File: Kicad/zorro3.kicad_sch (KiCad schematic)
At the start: 13 parts, among them CN1 Zorro3, U1 SN74ABT16543DGGR, U2 SN74ABT16543DGGR, U3 SN74ABT16543DGGR, U4 SN74ABT16543DGGR, U5 74LVC07APW_118, U6 SN74ABT16245ADGGR

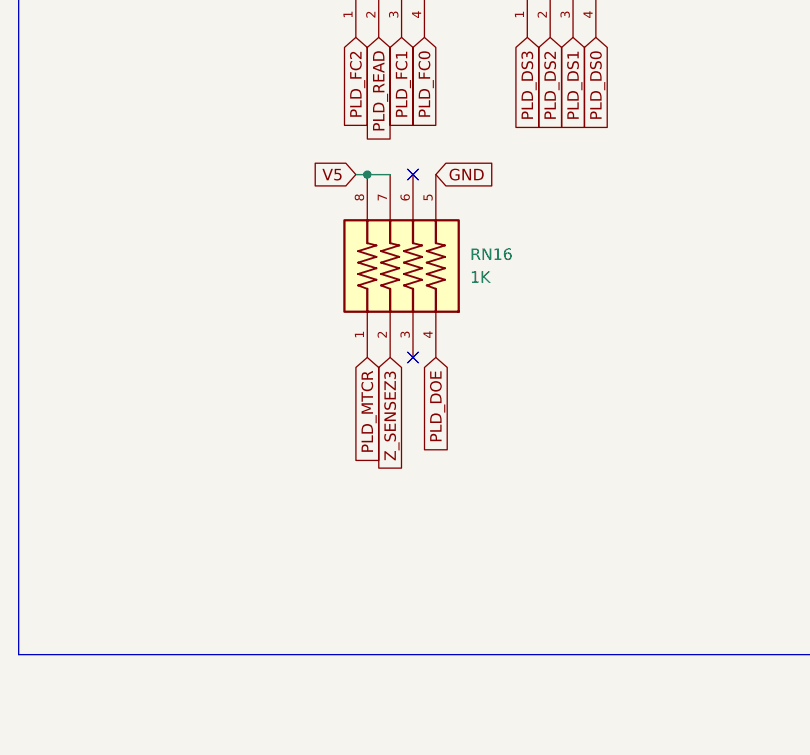
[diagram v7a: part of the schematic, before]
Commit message: Kicad: Pin swaps on RN10 and RN16
Fixes issue #1 and issue #2
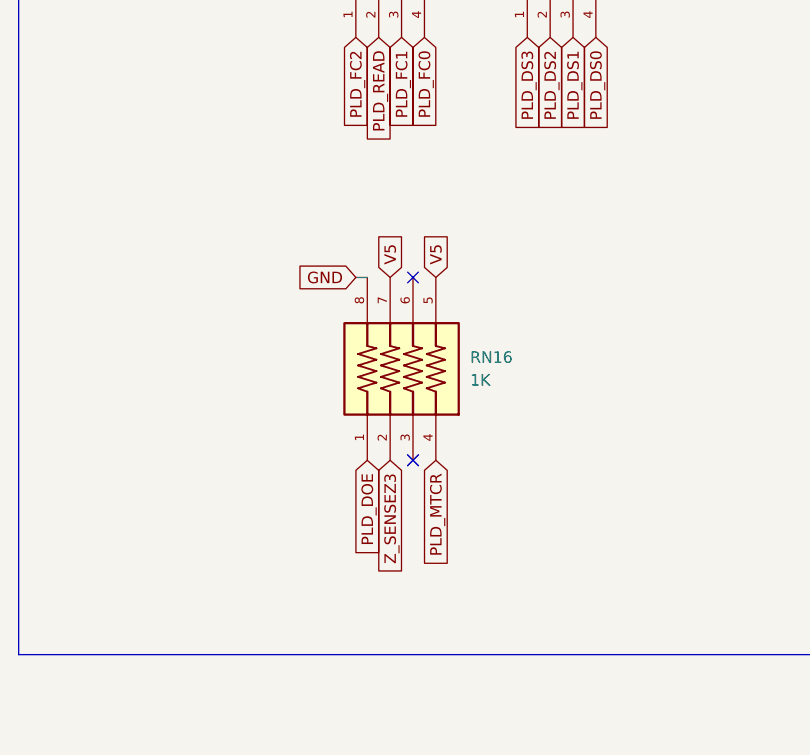
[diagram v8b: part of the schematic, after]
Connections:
- net GND: now also RN16.8; no longer RN16.5
- net PLD_DOE: now also RN16.1; no longer RN16.4
- net PLD_MTCR: now also RN16.4; no longer RN16.1
- net V5: now also RN16.5; no longer RN16.8
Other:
- moved on the sheet: RN16
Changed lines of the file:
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@@
 	)
 	(junction
-		(at 255.27 143.51)
-		(diameter 0)
-		(color 0 0 0 0)
-	)
-	(junction
 		(at 345.44 175.26)
 		(diameter 0)
@@
 	)
 	(no_connect
-		(at 260.35 143.51)
+		(at 260.35 154.94)
 	)
 	(no_connect
@@
 	)
 	(no_connect
-		(at 260.35 163.83)
+		(at 260.35 175.26)
 	)
 	(no_connect
@@
 	(wire
 		(pts
-			(xy 254 143.51) (xy 255.27 143.51)
+			(xy 254 154.94) (xy 255.27 154.94)
 		)
 		(stroke
@@
 	(wire
 		(pts
-			(xy 255.27 143.51) (xy 257.81 143.51)
-		)
-		(stroke
-			(width 0)
-			(type default)
-		)
-	)
-	(wire
-		(pts
 			(xy 232.41 72.39) (xy 237.49 72.39)
 		)
@@
 		)
 	)
+	(global_label "V5"
+		(shape input)
+		(at 262.89 154.94 90)
+		(fields_autoplaced yes)
+		(effects
+			(font
+				(size 1.27 1.27)
+			)
+			(justify left)
+		)
+		(property "Intersheetrefs" "${INTERSHEET_REFS}"
+			(at 262.89 149.6567 90)
+			(effects
+				(font
+					(size 1.27 1.27)
+				)
+				(justify left)
+				(hide yes)
+			)
+		)
+	)
 	(global_label "D23"
 		(shape input)
@@
 		)
 	)
-	(global_label "PLD_MTCR"
-		(shape input)
-		(at 255.27 163.83 270)
-		(fields_autoplaced yes)
-		(effects
-			(font
-				(size 1.27 1.27)
-			)
-			(justify right)
-		)
-		(property "Intersheetrefs" "${INTERSHEET_REFS}"
-			(at 255.27 176.3099 90)
-			(effects
-				(font
-					(size 1.27 1.27)
-				)
-				(justify right)
-				(hide yes)
-			)
-		)
-	)
 	(global_label "Z_MTCR"
 		(shape input)
@@
 		)
 	)
-	(global_label "GND"
-		(shape input)
-		(at 262.89 143.51 0)
-		(fields_autoplaced yes)
-		(effects
-			(font
-				(size 1.27 1.27)
-			)
-			(justify left)
-		)
-		(property "Intersheetrefs" "${INTERSHEET_REFS}"
-			(at 269.7457 143.51 0)
-			(effects
-				(font
-					(size 1.27 1.27)
-				)
-				(justify left)
-				(hide yes)
-			)
-		)
-	)
 	(global_label "PLD_FCS"
 		(shape input)
@@
 		)
 	)
+	(global_label "V5"
+		(shape input)
+		(at 257.81 154.94 90)
+		(fields_autoplaced yes)
+		(effects
+			(font
+				(size 1.27 1.27)
+			)
+			(justify left)
+		)
+		(property "Intersheetrefs" "${INTERSHEET_REFS}"
+			(at 257.81 149.6567 90)
+			(effects
+				(font
+					(size 1.27 1.27)
+				)
+				(justify left)
+				(hide yes)
+			)
+		)
+	)
 	(global_label "A25"
 		(shape input)
@@
 		)
 	)
+	(global_label "PLD_MTCR"
+		(shape input)
+		(at 262.89 175.26 270)
+		(fields_autoplaced yes)
+		(effects
+			(font
+				(size 1.27 1.27)
+			)
+			(justify right)
+		)
+		(property "Intersheetrefs" "${INTERSHEET_REFS}"
+			(at 262.89 187.7399 90)
+			(effects
+				(font
+					(size 1.27 1.27)
+				)
+				(justify right)
+				(hide yes)
+			)
+		)
+	)
 	(global_label "GND"
 		(shape input)
@@
 		)
 	)
+	(global_label "PLD_DOE"
+		(shape input)
+		(at 255.27 175.26 270)
+		(fields_autoplaced yes)
+		(effects
+			(font
+				(size 1.27 1.27)
+			)
+			(justify right)
+		)
+		(property "Intersheetrefs" "${INTERSHEET_REFS}"
+			(at 255.27 186.5304 90)
+			(effects
+				(font
+					(size 1.27 1.27)
+				)
+				(justify right)
+				(hide yes)
+			)
+		)
+	)
 	(global_label "D5"
 		(shape input)
@@
 	(global_label "Z_SENSEZ3"
 		(shape input)
-		(at 257.81 163.83 270)
+		(at 257.81 175.26 270)
 		(fields_autoplaced yes)
 		(effects
@@
 		)
 		(property "Intersheetrefs" "${INTERSHEET_REFS}"
-			(at 257.81 177.4588 90)
+			(at 257.81 188.8888 90)
 			(effects
 				(font
@@
 		)
 	)
+	(global_label "GND"
+		(shape input)
+		(at 254 154.94 180)
+		(fields_autoplaced yes)
+		(effects
+			(font
+				(size 1.27 1.27)
+			)
+			(justify right)
+		)
+		(property "Intersheetrefs" "${INTERSHEET_REFS}"
+			(at 247.1443 154.94 0)
+			(effects
+				(font
+					(size 1.27 1.27)
+				)
+				(justify right)
+				(hide yes)
+			)
+		)
+	)
 	(global_label "A17"
 		(shape input)
@@
 	(global_label "V5"
 		(shape input)
-		(at 254 143.51 180)
-		(fields_autoplaced yes)
-		(effects
-			(font
-				(size 1.27 1.27)
-			)
-			(justify right)
-		)
-		(property "Intersheetrefs" "${INTERSHEET_REFS}"
-			(at 248.7167 143.51 0)
-			(effects
-				(font
-					(size 1.27 1.27)
-				)
-				(justify right)
-				(hide yes)
-			)
-		)
-	)
-	(global_label "V5"
-		(shape input)
 		(at 370.84 147.32 0)
 		(fields_autoplaced yes)
@@
 		)
 	)
-	(global_label "PLD_DOE"
-		(shape input)
-		(at 262.89 163.83 270)
-		(fields_autoplaced yes)
-		(effects
-			(font
-				(size 1.27 1.27)
-			)
-			(justify right)
-		)
-		(property "Intersheetrefs" "${INTERSHEET_REFS}"
-			(at 262.89 175.1004 90)
-			(effects
-				(font
-					(size 1.27 1.27)
-				)
-				(justify right)
-				(hide yes)
-			)
-		)
-	)
 	(global_label "Z_D17"
 		(shape input)
@@
 	(symbol
 		(lib_id "YC324-FK-071KL:YC324-FK-071KL")
-		(at 260.35 153.67 90)
+		(at 260.35 165.1 90)
 		(unit 1)
 		(exclude_from_sim no)
@@
 		(fields_autoplaced yes)
 		(property "Reference" "RN16"
-			(at 266.7 152.3999 90)
+			(at 266.7 163.8299 90)
 			(effects
 				(font
@@
 		)
 		(property "Value" "1K"
-			(at 266.7 154.9399 90)
+			(at 266.7 166.3699 90)
 			(effects
 				(font
@@
 		)
 		(property "Footprint" "CAY16_102J4LF:BO_CAY16"
-			(at 260.35 153.67 0)
+			(at 260.35 165.1 0)
 			(effects
 				(font
@@
 		)
 		(property "Datasheet" ""
-			(at 260.35 153.67 0)
+			(at 260.35 165.1 0)
 			(effects
 				(font
@@
 		)
 		(property "Description" ""
-			(at 260.35 153.67 0)
+			(at 260.35 165.1 0)
 			(effects
 				(font
@@
 		)
 		(property "MAXIMUM_PACKAGE_HEIGHT" "0.7 mm"
-			(at 260.35 153.67 0)
+			(at 260.35 165.1 0)
 			(effects
 				(font
@@
 		)
 		(property "PARTREV" "V.9"
-			(at 260.35 153.67 0)
+			(at 260.35 165.1 0)
 			(effects
 				(font
@@
 		)
 		(property "MANUFACTURER" "Yageo"
-			(at 260.35 153.67 0)
+			(at 260.35 165.1 0)
 			(effects
 				(font
@@
 		)
 		(property "SNAPEDA_PACKAGE_ID" "22941"
-			(at 260.35 153.67 0)
+			(at 260.35 165.1 0)
 			(effects
 				(font
@@
 		)
 		(property "STANDARD" "IPC 7351B"
-			(at 260.35 153.67 0)
+			(at 260.35 165.1 0)
 			(effects
 				(font
